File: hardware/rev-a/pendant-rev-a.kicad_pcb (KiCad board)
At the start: 4 copper layers, 20 x 34 mm, 92 parts, among them J1 USB4105-GF-A (candidate), J2 S2B-PH-SM4-TB(LF)(SN) / DTP40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, J3 SWD pads, Q1 DMP2035U (candidate; power pa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, Q2 2N7002 (charge inhibit), Q3 2N7002 (VBUS detect), SW1 B3U-1000P (candidate), U1 STM32U535RCT6, U10 TPS22916CYFPR, U11 CSNP32GCR01-BOW, U2 USBLC6-2SC6, U3 BQ25101YFPR, U4 TPS7A0230PDBVR, U5 TPS7A0233PDBVR, U6 TPS7A0218PDBVR, U7 MAX17048G+T10, U8 T5838, U9 TXS0104EYZTR, Y1 32.768kHz CL=7pF TBD

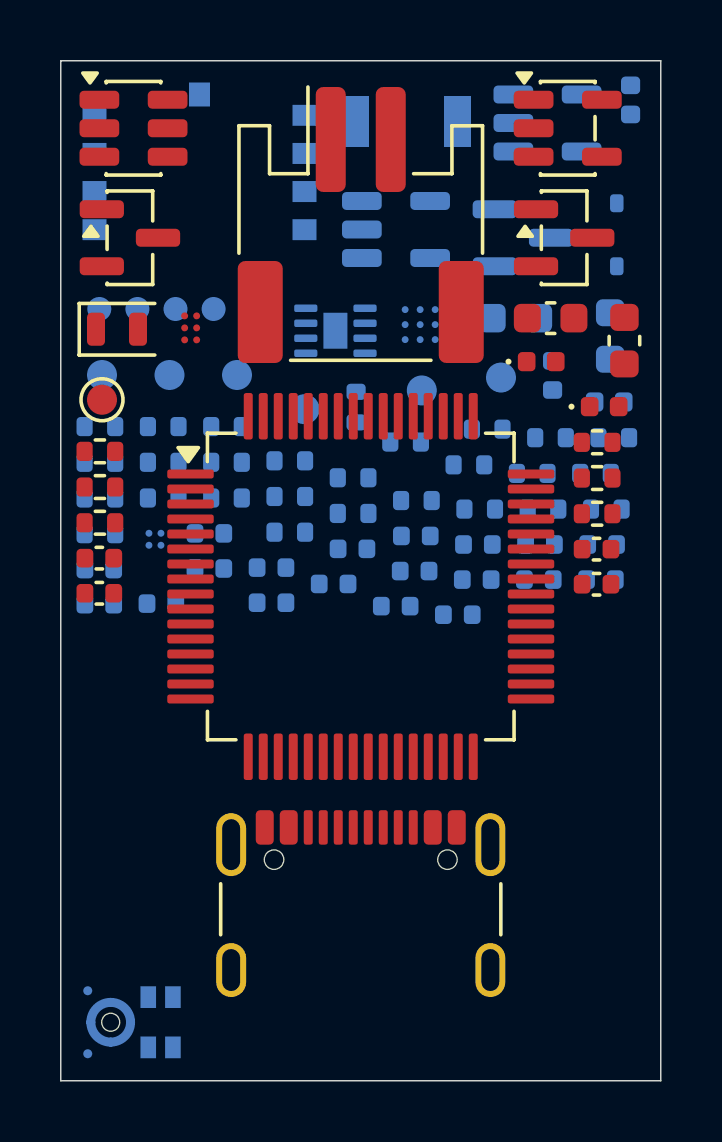
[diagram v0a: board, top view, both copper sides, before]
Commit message: Advance v1 sourcing audit, standard SWD connection and audio profile validation
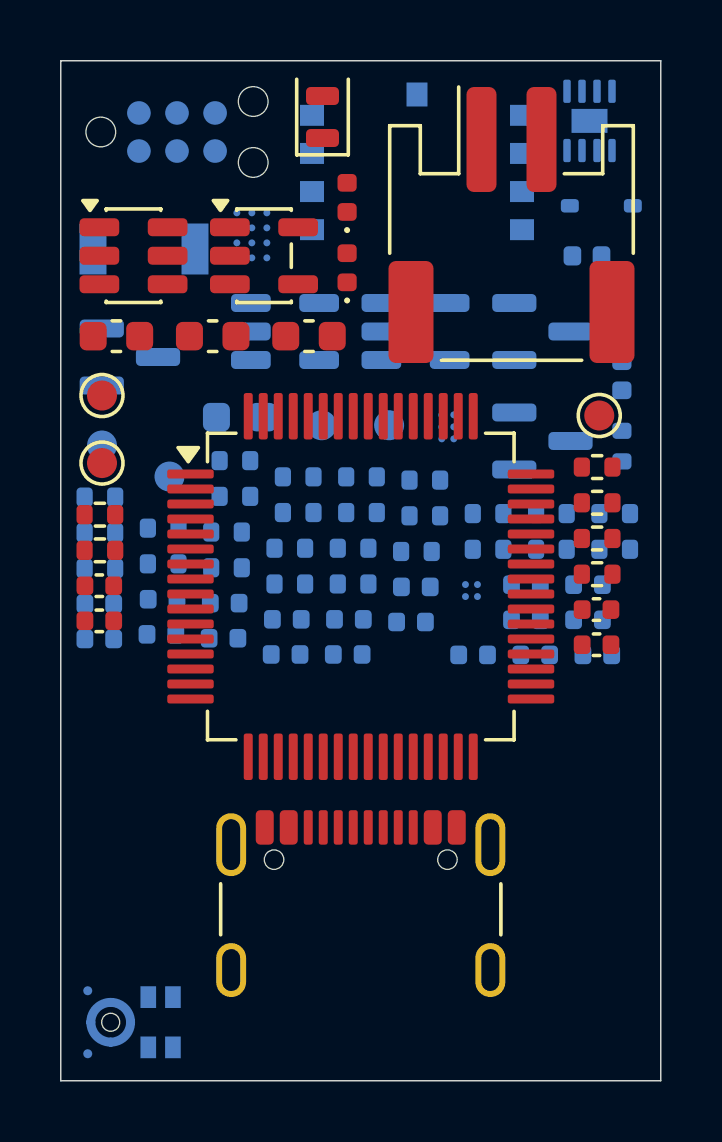
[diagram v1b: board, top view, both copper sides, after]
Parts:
- C15, C16, C3, C4, D1, D4, R14, R25, R3, TP1, TP2, U4: moved to F.Cu
- C20, C27, C9, D3, D6, Q1, Q2, R10, R18, R29, U3, U5: moved to B.Cu
- J3: value SWD pads -> TC2030-CTX-NL-STDC14 target pads; footprint Pendant:SWD_5Pad_Pogo -> Connector:Tag-Connect_TC2030-IDC-NL_2x03_P1.27mm_Vertical
- moved C20 16.7 mm to (101.3, 119.3)
- moved C9 16.7 mm to (101.3, 118.1)
- moved R18 16.7 mm to (101.3, 115.7)
- moved R29 16.7 mm to (101.3, 116.9)
- moved C10 16.7 mm to (117.9, 118.3)
- moved C21 16.7 mm to (117.9, 119.5)
- moved R19 16.7 mm to (117.9, 115.9)
- moved R30 16.7 mm to (117.9, 117.1)
- moved R27 14.9 mm to (103.4, 116.8)
- moved C7 14.8 mm to (103.4, 118.0)
- moved C18 14.8 mm to (103.4, 119.1)
- moved R3 14.5 mm to (117.9, 113.5)
- moved R16 14.5 mm to (103.4, 115.6)
- moved TP2 14.4 mm to (118.0, 111.8)
- moved C13 14.3 mm to (115.5, 118.6)
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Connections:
- J3 pad 3: GND -> NRST
- J3 pad 5: NRST -> GND
